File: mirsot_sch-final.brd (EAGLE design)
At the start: 60 x 60 mm, 43 parts, among them IC1 7805DT, U2 ATMEGA16-16AC, U4 DRV8833PWPR

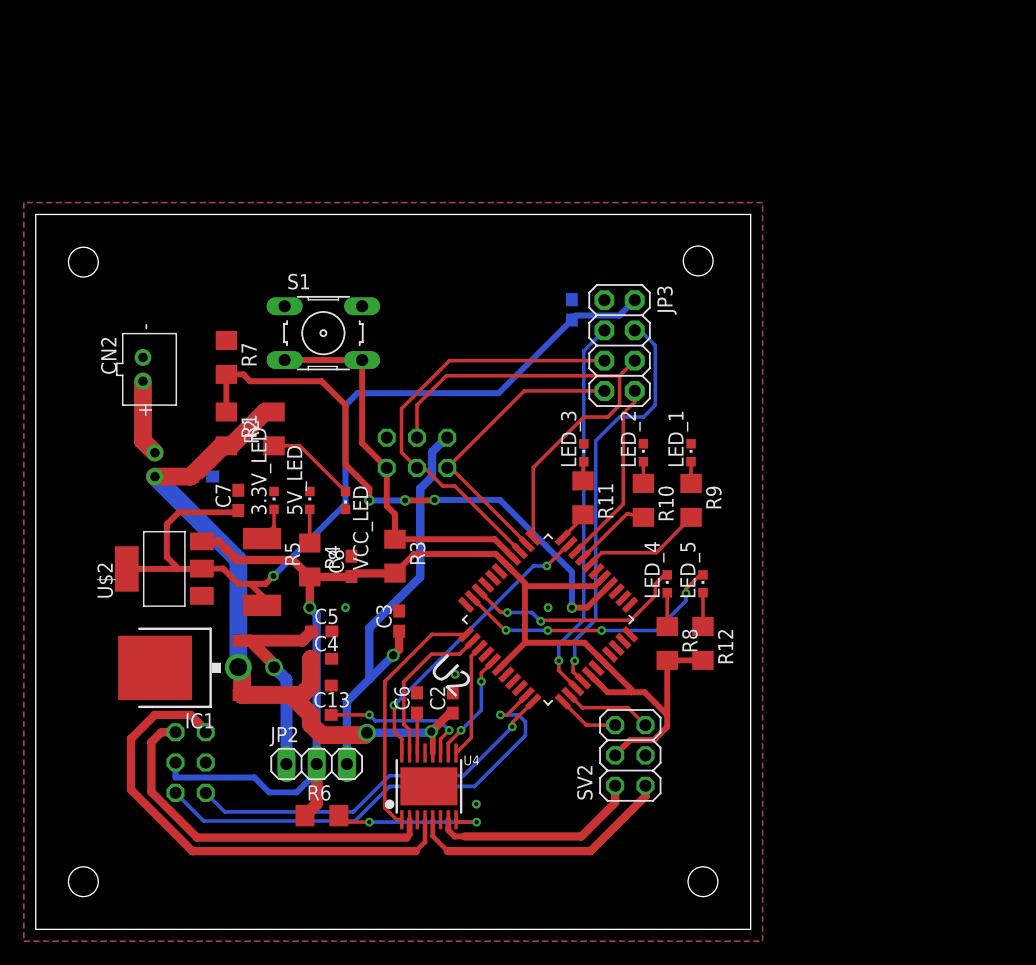
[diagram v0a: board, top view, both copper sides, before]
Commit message: shifted from smd to tht
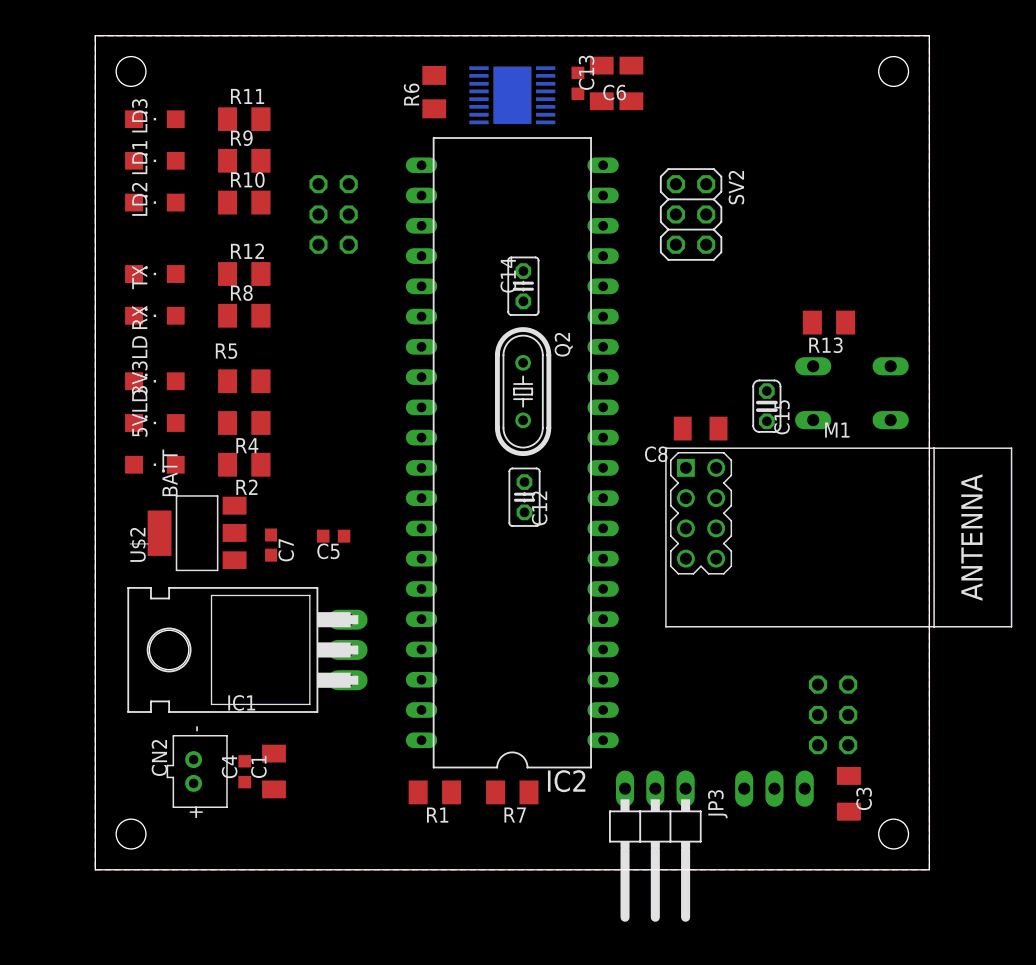
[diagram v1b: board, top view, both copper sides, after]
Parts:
- removed 3.3V_LED, 5V_LED, VCC_LED: RED, adafruit:CHIPLED_0603
- removed C10: 10u, rcl:C0603
- removed C2: 100n, rcl:C0603
- removed CN1: (no value), adafruit:JST-PH-2-THM
- removed LED_1, LED_2, LED_3, LED_4, LED_5: GREEN, adafruit:CHIPLED_0603
- removed R3: 43k, rcl:R1206
- removed S1: (no value), switch-omron:B3F-10XX
- removed U2: ATMEGA16-16AC, ATMEGA16-16AC:QFP80P1200X1200X120-44N
- added 3V3LD, 5VLD, BATT: RED, led:SML1206
- added C12, C14: 22pF, rcl:C025-025X050
- added C15: 100n, rcl:C025-024X044
- added IC2: MEGA16-P, atmel:DIL40
- added LD1, LD2, LD3: GREEN, led:SML1206
- added M1: WIRELESS-NRF24L01, diy-modules:WIRELESS-NRF24L01
- added Q2: (no value), crystal:HC49/S
- added R13: 43k, rcl:M1206
- added RX: BLUE, led:SML1206
- added S2: (no value), switch-omron:B3F-10XX
- added TX: YELLOW, led:SML1206
- C1, C13, C3, C6: device rcl:C0603 -> rcl:C1206K
- C4, C5, C9: device rcl:C0603 -> rcl:C0603K
- C8: value 100n -> 10u; device rcl:C0603 -> rcl:C1206K
- IC1: value 7805DT -> 7805T; device linear:TO252 -> linear:TO220H
- JP1: device pinhead:2X03 -> pinhead:2X03/90
- JP2: device pinhead:1X03 -> pinhead:1X03/90
- JP3: device adafruit:2X04 -> pinhead:1X03/90
- R1, R10, R11, R12, R2, R4, R6, R7, R8, R9: device rcl:R1206 -> rcl:M1206
- R5: device rcl:R2512 -> rcl:M1206
- moved R6 61.4 mm to (28.4, 65.3), turned to 90 degrees
- moved U4 58.4 mm to (35.0, 65.0), flipped to the bottom, turned to 90 degrees
- moved C13 58.0 mm to (42.5, 66.0), turned to 90 degrees
- moved C6 55.0 mm to (45.0, 66.0)
- moved C9 54.9 mm to (40.5, 66.0), turned to 90 degrees
- moved R12 49.4 mm to (12.5, 50.0), turned to 0 degrees
- moved SV1 47.5 mm to (20.0, 55.0)
- moved R9 47.1 mm to (12.5, 59.5), turned to 0 degrees
- moved SV2 45.7 mm to (50.0, 55.0), turned to 270 degrees
- moved JP1 45.7 mm to (67.0, 13.0), turned to 90 degrees
- moved R8 44.9 mm to (12.5, 46.5), turned to 0 degrees
- moved R7 43.7 mm to (35.0, 6.50), turned to 180 degrees
- moved R11 42.6 mm to (12.5, 63.0), turned to 0 degrees
- moved R10 41.8 mm to (12.5, 56.0), turned to 0 degrees
- moved JP3 41.1 mm to (47.0, 3.00), turned to 180 degrees
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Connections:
- removed net N$1: CN1.2, CN2.1
- removed net RX_LED: LED_4.C, U2.9
- removed net TX_LED: LED_5.C, U2.10
- new net GND1: C15.2
- new net N$12: C12.1, IC2.12, Q2.2
- new net N$13: C14.1, IC2.13, Q2.1
- new net N$14: C12.2, C14.2
- new net RESET: JP1.5, JP3.2
- new net RX: IC2.14, JP3.1, RX.C
- new net TX: IC2.15, JP3.3, TX.C
- net +3V3: now also C8.1, M1.2; no longer C10.1, JP3.2
- net +5V: now also C15.1, IC2.10, IC2.30, IC2.32, R13.2; no longer C8.1, R3.2, U2.17, U2.27, U2.29, U2.38, U2.5
- net +5V_SUPPLY: now also IC1.3; no longer IC1.2
- net AIN1: now also IC2.4; no longer U2.43
- net AIN2: now also IC2.18; no longer U2.13
- net BIN1: now also IC2.19; no longer U2.14
- net BIN2: now also IC2.21; no longer U2.16
- net CE: now also IC2.28, M1.3; no longer JP3.3, U2.25
- net CSN: now also IC2.29, M1.4; no longer JP3.4, U2.26
- net ENB: now also IC2.17; no longer U2.12
- net ENCD_MA_1: now also IC2.24; no longer U2.21
- net ENCD_MA_2: now also IC2.25; no longer U2.22
- net ENCD_MB_1: now also IC2.26; no longer U2.23
- net ENCD_MB_2: now also IC2.27; no longer U2.24
- net GND: now also 3V3LD.C, 5VLD.C, BATT.C, IC1.2, IC2.11, IC2.31, LD1.C, LD2.C, LD3.C, M1.1, S2.1, S2.2; no longer 3.3V_LED.C, 5V_LED.C, C10.2, C2.2, IC1.3, JP3.1, LED_1.C, LED_2.C, LED_3.C, S1.1, S1.2, U2.18, U2.28, U2.39, U2.6, VCC_LED.C
- net IRQ: now also IC2.3, M1.8; no longer JP3.8, U2.42
- net LED_1: now also IC2.1; no longer U2.40
- net LED_2: now also IC2.2; no longer U2.41
- net LED_3: now also IC2.5; no longer U2.44
- net MISO: now also IC2.7, M1.7; no longer JP3.7, U2.2
- net MOSI: now also IC2.6, M1.6; no longer JP3.6, U2.1
- net N$10: now also RX.A; no longer LED_4.A
- net N$11: now also TX.A; no longer LED_5.A
- net N$2: now also BATT.A; no longer VCC_LED.A
- net N$3: now also LD1.A; no longer LED_1.A
- net N$4: now also LD2.A; no longer LED_2.A
- net N$5: now also 5VLD.A; no longer 5V_LED.A
- net N$6: now also 3V3LD.A; no longer 3.3V_LED.A
- net N$9: now also LD3.A; no longer LED_3.A
- net RST: now also IC2.9, R13.1, S2.3, S2.4; no longer JP1.5, R3.1, S1.3, S1.4, U2.4
- net SCK: now also IC2.8, M1.5; no longer JP3.5, U2.3
- net VCC: now also CN2.1; no longer C2.1, CN1.1
- net VCC_REF: now also IC2.40; no longer U2.37
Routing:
- net +5V: track 113.3 -> 0.00 mm, vias 1 -> 0
- net +3V3: track 70.7 -> 0.00 mm, vias 1 -> 0
- net VCC: track 67.6 -> 0.00 mm, vias 3 -> 0
- net VCC_REF: track 49.6 -> 0.00 mm, vias 4 -> 0
- net AOUT-: track 41.1 -> 0.00 mm
- net MOSI: track 40.3 -> 0.00 mm
- net ENCD_MA_1: track 39.7 -> 0.00 mm, vias 1 -> 0
- net +5V_PROG: track 36.0 -> 0.00 mm, vias 1 -> 0
- net SCK: track 35.7 -> 0.00 mm
- net CSN: track 34.8 -> 0.00 mm, vias 1 -> 0
- net RST: track 33.2 -> 0.00 mm
- net CE: track 32.2 -> 0.00 mm, vias 1 -> 0
- net ENCD_MA_2: track 32.2 -> 0.00 mm, vias 1 -> 0
- net AOUT+: track 31.2 -> 0.00 mm
- net MISO: track 25.2 -> 0.00 mm
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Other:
- board size 60 x 60 mm -> 70 x 70 mm

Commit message: added drv8833 module
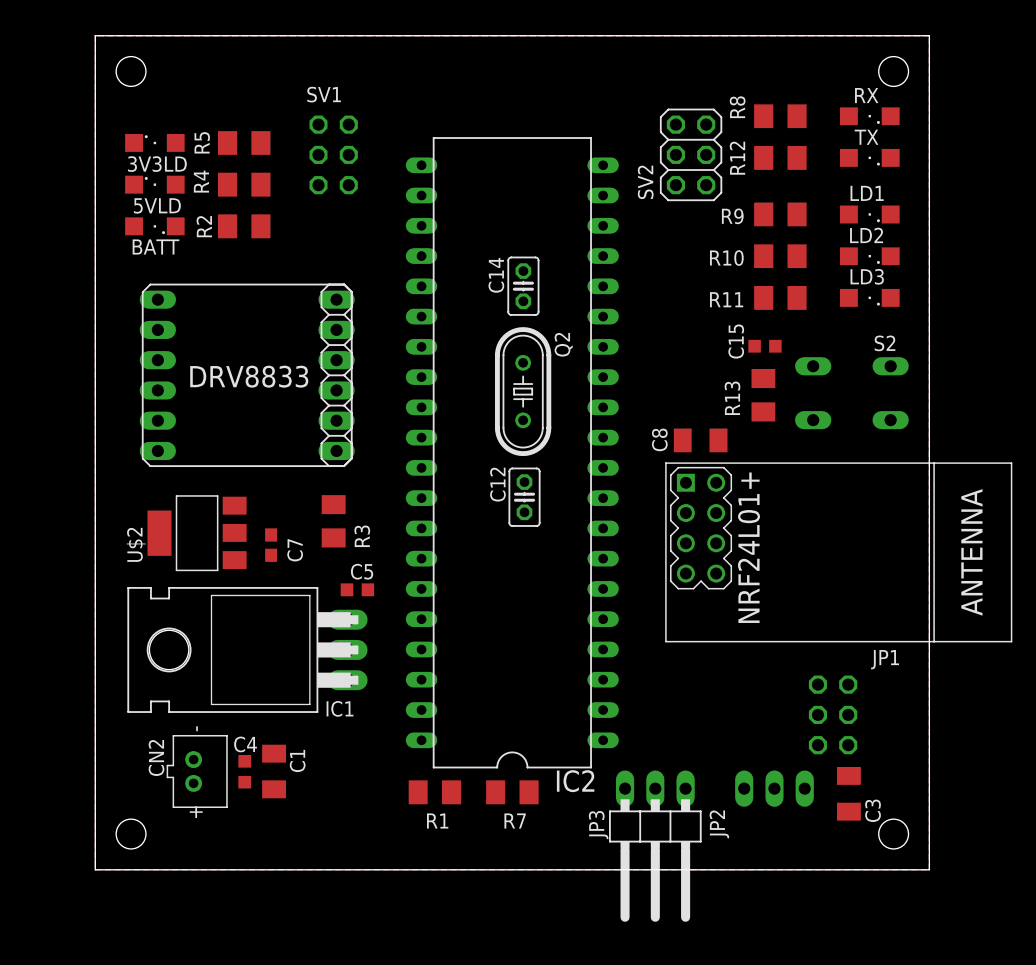
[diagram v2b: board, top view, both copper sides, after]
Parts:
- removed C13: 0.01u, rcl:C1206K
- removed C6: 2.2u, rcl:C1206K
- removed C9: 10u, rcl:C0603K
- removed R6: 43k, rcl:M1206
- removed U4: DRV8833PWPR, microbuilder:HTSSOP16
- added JP4, JP5: (no value), pinhead:1X06
- added R3: 43k, rcl:M1206
- C15: device rcl:C025-024X044 -> rcl:C0603K
- moved RX 62.3 mm to (65.0, 63.2), turned to 180 degrees
- moved LD3 61.8 mm to (65.0, 48.0), turned to 180 degrees
- moved TX 60.8 mm to (65.0, 59.8), turned to 180 degrees
- moved LD1 60.2 mm to (65.0, 55.0), turned to 180 degrees
- moved LD2 60.2 mm to (65.0, 51.5), turned to 180 degrees
- moved R8 48.0 mm to (57.5, 63.2), turned to 180 degrees
- moved R11 47.4 mm to (57.5, 48.0), turned to 180 degrees
- moved R12 46.0 mm to (57.5, 59.8), turned to 180 degrees
- moved R10 45.2 mm to (57.5, 51.5), turned to 180 degrees
- moved R9 45.2 mm to (57.5, 55.0), turned to 180 degrees
- moved 3V3LD 20.0 mm to (5.00, 61.0)
- moved 5VLD 20.0 mm to (5.00, 57.5)
- moved BATT 20.0 mm to (5.00, 54.0)
- moved R2 20.0 mm to (12.5, 54.0)
- moved R4 20.0 mm to (12.5, 57.5)
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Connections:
- removed net N$7: C13.2, U4.11
- removed net N$8: C6.1, U4.14
- removed net NFAULT: R6.2, U4.8
- new net N$1: JP4.6, R3.2
- net +5V: now also R3.1; no longer R6.1
- net AIN1: now also JP5.6; no longer U4.16
- net AIN2: now also JP5.5; no longer U4.15
- net AOUT+: now also JP4.2; no longer U4.2
- net AOUT-: now also JP4.3; no longer U4.4
- net BIN1: now also JP5.2; no longer U4.9
- net BIN2: now also JP5.1; no longer U4.10
- net BOUT+: now also JP4.4; no longer U4.7
- net BOUT-: now also JP4.5; no longer U4.5
- net ENB: now also JP4.1; no longer U4.1
- net GND: now also JP5.3; no longer C6.2, C9.2, U4.13, U4.3, U4.6, U4.PPAD
- net VCC: now also JP5.4; no longer C13.1, C9.1, U4.12
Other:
- board text added: "DRV8833"
- board text added: "NRF24L01+"

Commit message: Routing Done
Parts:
- moved R13 2.69 mm to (55.1, 42.3), turned to 180 degrees
- moved C15 2.02 mm to (54.5, 44.9)
- moved 3V3LD 0.75 mm to (5.75, 61.0)
- moved 5VLD 0.75 mm to (5.75, 57.5)
- moved BATT 0.75 mm to (5.75, 54.0), turned to 0 degrees
- moved LD1 0.75 mm to (64.2, 55.0)
- moved LD2 0.75 mm to (64.2, 51.5)
- moved LD3 0.75 mm to (64.2, 48.0)
- moved RX 0.75 mm to (64.2, 63.2)
- moved TX 0.75 mm to (64.2, 59.8)
- turned CN2 to 90 degrees
- turned R2 to 0 degrees
- turned R4 to 0 degrees
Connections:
- removed net GND1: C15.2
- net ENB: now also IC2.22; no longer IC2.17
- net ENCD_MA_1: now also IC2.25; no longer IC2.24
- net ENCD_MA_2: now also IC2.24; no longer IC2.25
- net ENCD_MB_1: now also IC2.23; no longer IC2.26
- net ENCD_MB_2: now also IC2.26; no longer IC2.27
- net GND: now also C15.2
- net LED_1: now also IC2.20; no longer IC2.1
- net LED_2: now also IC2.17; no longer IC2.2
- net LED_3: now also IC2.16; no longer IC2.5
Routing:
- net +3V3: track 0.00 -> 116.8 mm, vias 0 -> 4
- net RX: track 0.00 -> 94.5 mm, vias 0 -> 1
- net TX: track 0.00 -> 93.1 mm, vias 0 -> 2
- net BOUT+: track 0.00 -> 91.5 mm
- net VCC: track 0.00 -> 83.3 mm, vias 0 -> 2
- net BOUT-: track 0.00 -> 74.1 mm, vias 0 -> 1
- net +5V_SUPPLY: track 0.00 -> 45.4 mm
- net +5V: track 0.00 -> 45.4 mm, vias 0 -> 9
- net CSN: track 0.00 -> 45.3 mm
- net ENB: track 0.00 -> 43.9 mm
- net SCK: track 0.00 -> 42.8 mm
- net MISO: track 0.00 -> 41.7 mm
- net MOSI: track 0.00 -> 34.8 mm
- net ENCD_MB_2: track 0.00 -> 34.7 mm
- net AOUT-: track 0.00 -> 34.4 mm
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- added copper zone on layer 16, net +5V
- removed copper zone on layer 16, net GND
